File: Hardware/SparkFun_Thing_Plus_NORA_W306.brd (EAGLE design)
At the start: 22.9 x 58.4 mm, 152 parts, among them J1 THING_PLUS_LOGICAL, J2 LiPo, J3 QWIIC_RA, J4 MICRO-SDFRICTION, J5 USB-C, J6 SWD, Q1 3.1A/30V/105mΩ, Q2 MBT3904DW1T1, U1 UBLOX_NORA_W306, U3 XC6222B331MR-G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

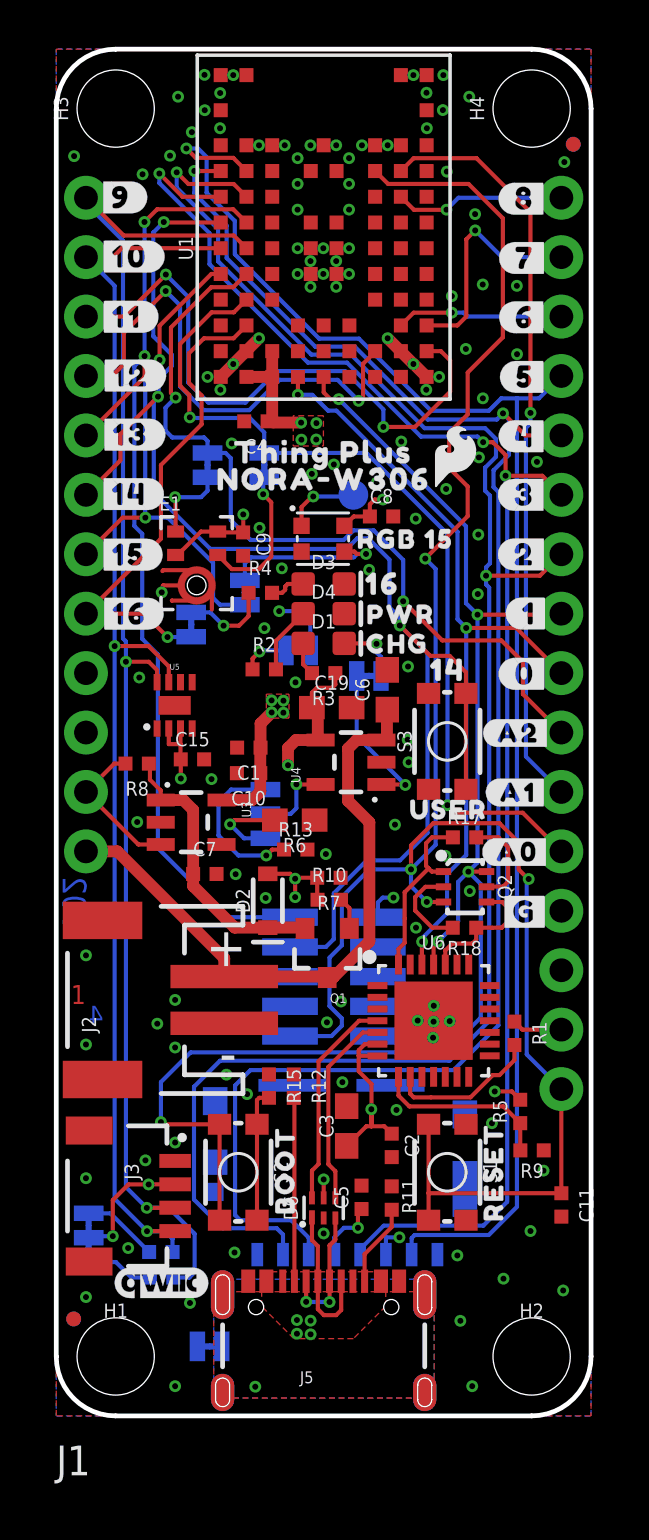
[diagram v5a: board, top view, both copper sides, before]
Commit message: nudged trace for better gnd flow
added gnd via near swd layer transfer
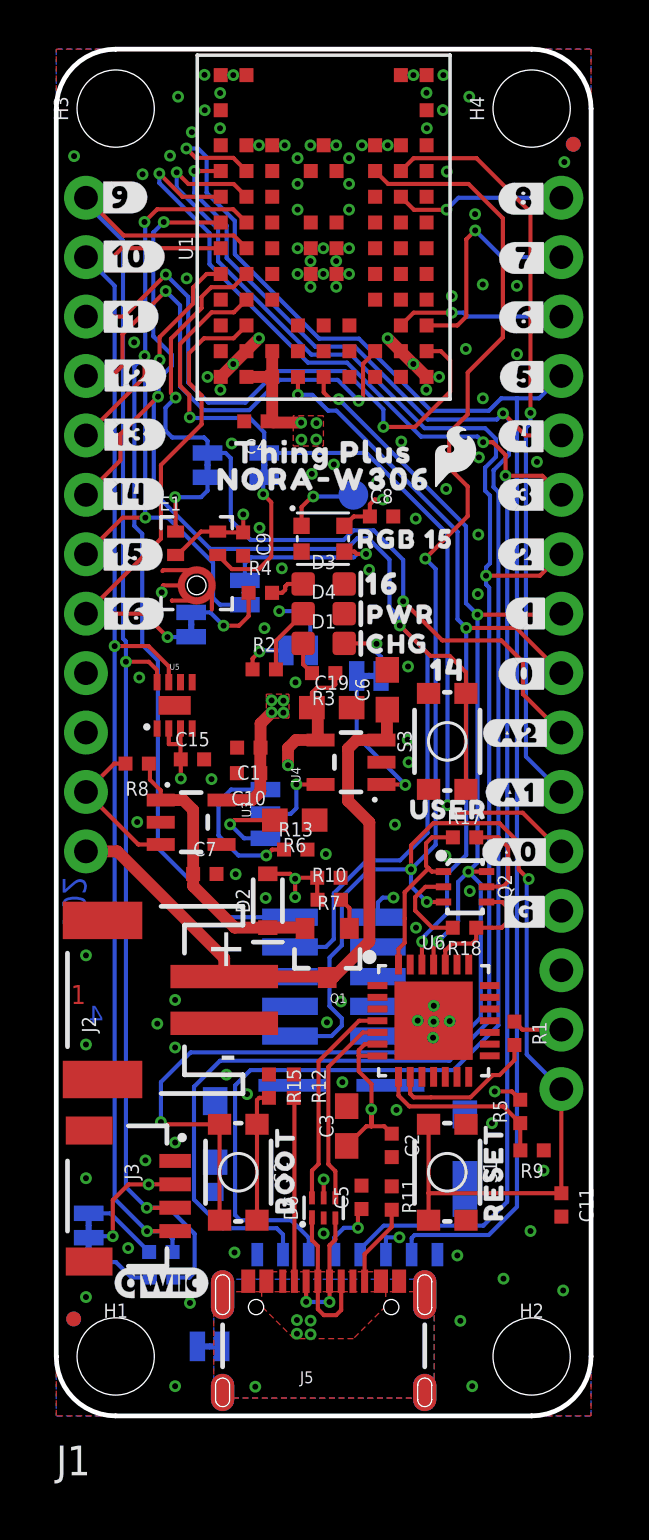
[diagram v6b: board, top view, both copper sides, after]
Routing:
- net GND: vias 120 -> 122
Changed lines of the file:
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@@
 <setting verticaltext="up"/>
 </settings>
-<grid distance="0.05" unitdist="inch" unit="inch" style="lines" multiple="1" display="yes" altdistance="0.005" altunitdist="inch" altunit="inch"/>
+<grid distance="0.05" unitdist="inch" unit="inch" style="lines" multiple="1" display="yes" altdistance="0.0001" altunitdist="inch" altunit="inch"/>
 <layers>
 <layer number="1" name="Top" color="4" fill="1" visible="yes" active="yes"/>
@@
 <contactref element="J6" pad="3"/>
 <contactref element="J6" pad="9"/>
+<via x="3.328578125" y="45.887196875" extent="1-16" drill="0.254"/>
+<via x="5.5739375" y="48.622778125" extent="1-16" drill="0.254"/>
 </signal>
 <signal name="V_USB">
@@
 <wire x1="1.27" y1="41.91" x2="1.277621875" y2="41.91" width="0.1778" layer="1"/>
 <wire x1="7.563759375" y1="51.577240625" x2="4.31291875" y2="51.577240625" width="0.1778" layer="1"/>
-<wire x1="3.774440625" y1="51.02860625" x2="3.7693625" y2="51.033684375" width="0.1778" layer="16"/>
-<wire x1="3.774440625" y1="45.300896875" x2="3.774440625" y2="51.02860625" width="0.1778" layer="16"/>
+<wire x1="3.80238125" y1="51.000665625" x2="3.7693625" y2="51.033684375" width="0.1778" layer="16"/>
+<wire x1="3.80238125" y1="51.000665625" x2="3.80238125" y2="45.3288375" width="0.1778" layer="16"/>
+<wire x1="3.774440625" y1="45.300896875" x2="3.80238125" y2="45.3288375" width="0.1778" layer="16"/>
 <contactref element="J6" pad="2"/>
 <wire x1="9.989421875" y1="21.31568125" x2="7.29741875" y2="21.31568125" width="0.1778" layer="16"/>
@@
 <wire x1="3.337559375" y1="44.864015625" x2="3.774440625" y2="45.300896875" width="0.1778" layer="16"/>
 <wire x1="7.29741875" y1="21.31568125" x2="4.3434" y2="24.2697" width="0.1778" layer="16"/>
-<wire x1="4.3434" y1="24.2697" x2="4.3434" y2="32.545021875" width="0.1778" layer="16"/>
-<wire x1="4.3434" y1="32.545021875" x2="3.67538125" y2="33.213040625" width="0.1778" layer="16"/>
-<wire x1="3.67538125" y1="33.213040625" x2="3.67538125" y2="37.70121875" width="0.1778" layer="16"/>
+<wire x1="4.3434" y1="24.2697" x2="4.3434" y2="32.291021875" width="0.1778" layer="16"/>
+<wire x1="4.3434" y1="32.291021875" x2="3.67538125" y2="32.959040625" width="0.1778" layer="16"/>
+<wire x1="3.67538125" y1="32.959040625" x2="3.67538125" y2="37.70121875" width="0.1778" layer="16"/>
 </signal>
 <signal name="PB22">
 <contactref element="U1" pad="E9"/>
 <contactref element="J1" pad="7"/>
-<wire x1="7.03" y1="48.811" x2="6.62921875" y2="48.811" width="0.1778" layer="1"/>
 <via x="3.8074625" y="38.3946375" extent="1-16" drill="0.254"/>
 <wire x1="3.8074625" y1="38.3946375" x2="4.770121875" y2="38.3946375" width="0.1778" layer="16"/>
@@
 <wire x1="2.8346375" y1="38.3946375" x2="3.8074625" y2="38.3946375" width="0.1778" layer="1"/>
 <via x="4.41705625" y="45.1358" extent="1-16" drill="0.254"/>
-<wire x1="4.41705625" y1="45.1358" x2="4.41705625" y2="46.5988375" width="0.1778" layer="1"/>
-<wire x1="4.41705625" y1="46.5988375" x2="6.62921875" y2="48.811" width="0.1778" layer="1"/>
 <wire x1="4.41705625" y1="45.1358" x2="3.799840625" y2="44.518584375" width="0.1778" layer="16"/>
 <wire x1="3.799840625" y1="44.518584375" x2="3.799840625" y2="38.402259375" width="0.1778" layer="16"/>
@@
 <wire x1="6.7030625" y1="36.461696875" x2="6.7030625" y2="34.965640625" width="0.1778" layer="16"/>
 <wire x1="6.7030625" y1="34.965640625" x2="6.9951625" y2="34.673540625" width="0.1778" layer="16"/>
+<wire x1="4.41705625" y1="45.1358" x2="4.41705625" y2="46.11115625" width="0.1778" layer="1"/>
+<wire x1="4.41705625" y1="46.11115625" x2="5.844540625" y2="47.538640625" width="0.1778" layer="1"/>
+<wire x1="5.844540625" y1="47.538640625" x2="5.844540625" y2="48.226978125" width="0.1778" layer="1"/>
+<wire x1="5.844540625" y1="48.226978125" x2="6.4285625" y2="48.811" width="0.1778" layer="1"/>
+<wire x1="6.4285625" y1="48.811" x2="7.03" y2="48.811" width="0.1778" layer="1"/>
 </signal>
 <signal name="PB2/DMIC_DATA">
@@
 <contactref element="JP2" pad="2"/>
 <wire x1="8.13" y1="48.811" x2="7.563759375" y2="48.244759375" width="0.1778" layer="1"/>
-<wire x1="6.624321875" y1="48.244759375" x2="4.9022" y2="46.5226375" width="0.1778" layer="1"/>
-<wire x1="4.9022" y1="46.5226375" x2="4.9022" y2="43.728640625" width="0.1778" layer="1"/>
+<wire x1="4.9022" y1="46.04258125" x2="4.9022" y2="43.728640625" width="0.1778" layer="1"/>
 <wire x1="4.9022" y1="43.728640625" x2="5.102859375" y2="43.52798125" width="0.1778" layer="1"/>
 <via x="5.102859375" y="43.52798125" extent="1-16" drill="0.254"/>
@@
 <wire x1="4.9606375" y1="41.821084375" x2="6.316971875" y2="41.821084375" width="0.1778" layer="16"/>
 <wire x1="6.316971875" y1="41.821084375" x2="6.31698125" y2="41.82109375" width="0.1778" layer="16"/>
+<wire x1="6.624321875" y1="48.244759375" x2="6.2103" y2="47.8307375" width="0.1778" layer="1"/>
+<wire x1="6.2103" y1="47.35068125" x2="4.9022" y2="46.04258125" width="0.1778" layer="1"/>
+<wire x1="6.2103" y1="47.8307375" x2="6.2103" y2="47.35068125" width="0.1778" layer="1"/>
 </signal>
 <signal name="PB23">
@@
 <wire x1="5.29081875" y1="47.4700625" x2="4.67868125" y2="48.0822" width="0.1778" layer="16"/>
 <via x="4.67868125" y="48.0822" extent="1-16" drill="0.254"/>
-<wire x1="4.67868125" y1="48.0822" x2="2.88798125" y2="46.2915" width="0.1778" layer="1"/>
-<wire x1="2.88798125" y1="46.2915" x2="2.88798125" y2="44.95291875" width="0.1778" layer="1"/>
-<wire x1="2.88798125" y1="44.95291875" x2="2.3850625" y2="44.45" width="0.1778" layer="1"/>
+<wire x1="4.67868125" y1="48.0822" x2="2.8321" y2="46.23561875" width="0.1778" layer="1"/>
+<wire x1="2.8321" y1="46.23561875" x2="2.8321" y2="44.8970375" width="0.1778" layer="1"/>
+<wire x1="2.8321" y1="44.8970375" x2="2.3850625" y2="44.45" width="0.1778" layer="1"/>
 <wire x1="2.3850625" y1="44.45" x2="1.27" y2="44.45" width="0.1778" layer="1"/>
 <wire x1="12.026896875" y1="44.284903125" x2="9.545325" y2="44.284903125" width="0.1778" layer="16"/>

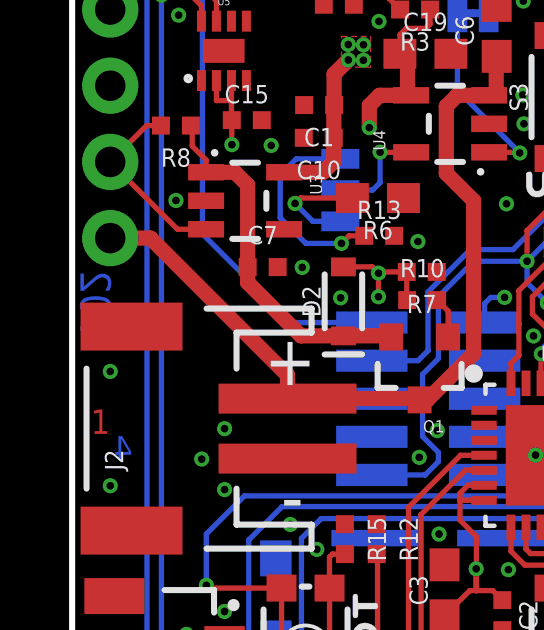
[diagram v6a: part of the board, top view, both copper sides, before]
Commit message: SWD header to DNP and bumped version to v03
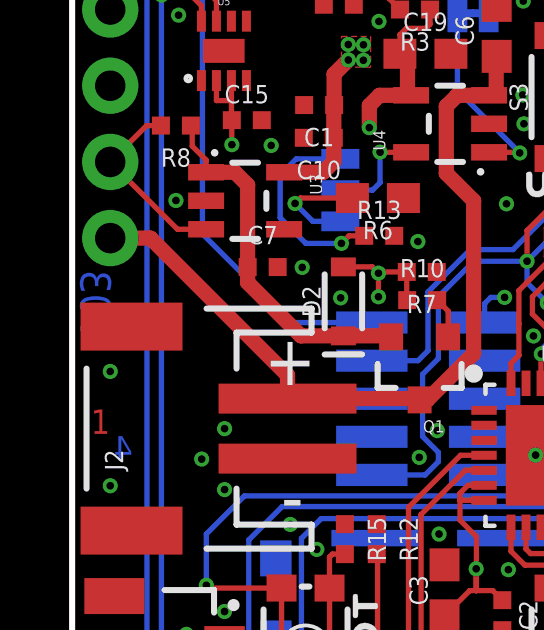
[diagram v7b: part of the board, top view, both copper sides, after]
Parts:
- J6: value SWD -> SWD (DNP)
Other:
- board text added: "v03"
- board text removed: "v02"
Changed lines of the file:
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@@
 <wire x1="2.54" y1="0" x2="20.32" y2="0" width="0.2032" layer="20"/>
 <wire x1="20.32" y1="0" x2="22.86" y2="2.54" width="0.2032" layer="20" curve="90"/>
-<text x="0.782321875" y="23.0759" size="1.016" layer="16" font="vector" ratio="20" rot="MR270" align="center-left">v02</text>
+<text x="0.782321875" y="23.0759" size="1.016" layer="16" font="vector" ratio="20" rot="MR270" align="center-left">v03</text>
 <text x="0.6223" y="17.604740625" size="0.8128" layer="1" font="vector" ratio="20">1</text>
 <text x="1.3843" y="17.604740625" size="0.8128" layer="2" font="vector" ratio="20">2</text>
@@
 <element name="U$74" library="output" package="#JP4#0" value="" x="5.78611875" y="31.480759375" smashed="yes" rot="MR90"/>
 <element name="U$73" library="output" package="RGB_155" value="" x="14.937740625" y="37.472621875" smashed="yes"/>
-<element name="J6" library="SparkFun-Connectors" package="2X5-SMD-UNSHROUDED" value="SWD" x="11.869421875" y="18.77568125" smashed="yes" rot="MR270">
+<element name="J6" library="SparkFun-Connectors" package="2X5-SMD-UNSHROUDED" value="SWD (DNP)" x="11.869421875" y="18.77568125" smashed="yes" rot="MR270">
 <attribute name="NAME" x="7.823421875" y="22.88168125" size="1.27" layer="26" rot="MR270"/>
 <attribute name="PROD_ID" value="CONN-15353" x="11.869421875" y="18.77568125" size="1.778" layer="28" font="vector" ratio="15" rot="MR270" display="off"/>

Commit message: removed paste from cortex debug SMD footprint (DNP)
-also bumped version to v04
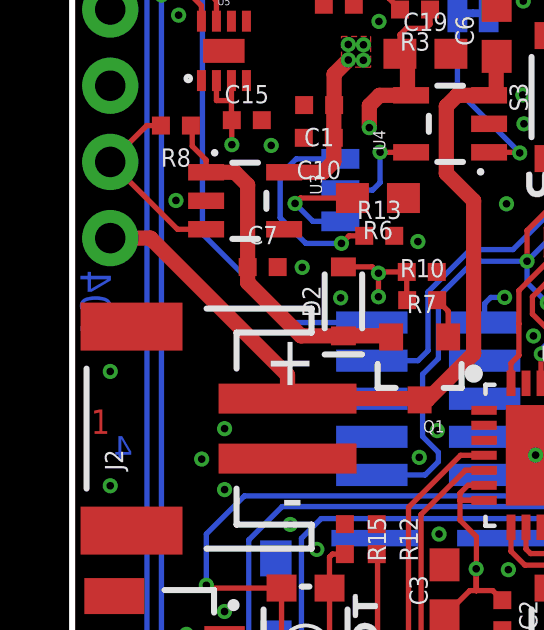
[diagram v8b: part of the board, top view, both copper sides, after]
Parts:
- J6: device SparkFun-Connectors:2X5-SMD-UNSHROUDED -> SparkFun-Connectors:2X5-SMD-UNSHROUDED_DNP_NO_PASTE
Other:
- board text added: "v04"
- board text removed: "v03"
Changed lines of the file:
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@@
 <setting verticaltext="up"/>
 </settings>
-<grid distance="0.05" unitdist="inch" unit="inch" style="lines" multiple="1" display="yes" altdistance="0.0001" altunitdist="inch" altunit="inch"/>
+<grid distance="0.05" unitdist="inch" unit="inch" style="lines" multiple="1" display="yes" altdistance="0.005" altunitdist="inch" altunit="inch"/>
 <layers>
 <layer number="1" name="Top" color="4" fill="1" visible="yes" active="yes"/>
@@
 <layer number="44" name="Drills" color="7" fill="1" visible="no" active="yes"/>
 <layer number="45" name="Holes" color="7" fill="1" visible="yes" active="yes"/>
-<layer number="46" name="Milling" color="3" fill="1" visible="yes" active="yes"/>
-<layer number="47" name="Measures" color="7" fill="1" visible="yes" active="yes"/>
+<layer number="46" name="Milling" color="3" fill="1" visible="no" active="yes"/>
+<layer number="47" name="Measures" color="7" fill="1" visible="no" active="yes"/>
 <layer number="48" name="Document" color="7" fill="1" visible="no" active="yes"/>
 <layer number="49" name="Reference" color="7" fill="1" visible="yes" active="yes"/>
@@
 <layer number="98" name="Guide" color="6" fill="1" visible="no" active="no"/>
 <layer number="99" name="SpiceOrder" color="7" fill="1" visible="no" active="no"/>
+<layer number="100" name="Muster" color="7" fill="1" visible="no" active="no"/>
 <layer number="101" name="Patch_Top" color="12" fill="4" visible="no" active="no"/>
 <layer number="102" name="Vscore" color="7" fill="1" visible="no" active="no"/>
@@
 <wire x1="2.54" y1="0" x2="20.32" y2="0" width="0.2032" layer="20"/>
 <wire x1="20.32" y1="0" x2="22.86" y2="2.54" width="0.2032" layer="20" curve="90"/>
-<text x="0.782321875" y="23.0759" size="1.016" layer="16" font="vector" ratio="20" rot="MR270" align="center-left">v03</text>
+<text x="0.782321875" y="23.0759" size="1.016" layer="16" font="vector" ratio="20" rot="MR270" align="center-left">v04</text>
 <text x="0.6223" y="17.604740625" size="0.8128" layer="1" font="vector" ratio="20">1</text>
 <text x="1.3843" y="17.604740625" size="0.8128" layer="2" font="vector" ratio="20">2</text>
@@
 <element name="U$74" library="output" package="#JP4#0" value="" x="5.78611875" y="31.480759375" smashed="yes" rot="MR90"/>
 <element name="U$73" library="output" package="RGB_155" value="" x="14.937740625" y="37.472621875" smashed="yes"/>
-<element name="J6" library="SparkFun-Connectors" package="2X5-SMD-UNSHROUDED" value="SWD (DNP)" x="11.869421875" y="18.77568125" smashed="yes" rot="MR270">
+<element name="J6" library="SparkFun-Connectors" package="2X5-SMD-UNSHROUDED_DNP_NO_PASTE" value="SWD (DNP)" x="11.869421875" y="18.77568125" smashed="yes" rot="MR270">
 <attribute name="NAME" x="7.823421875" y="22.88168125" size="1.27" layer="26" rot="MR270"/>
-<attribute name="PROD_ID" value="CONN-15353" x="11.869421875" y="18.77568125" size="1.778" layer="28" font="vector" ratio="15" rot="MR270" display="off"/>
 <attribute name="VALUE" x="17.649421875" y="22.58568125" size="1.27" layer="28" rot="MR270"/>
 </element>
